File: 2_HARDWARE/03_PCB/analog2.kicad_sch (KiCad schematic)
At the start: 21 parts, among them U22 TPL0401B-10, U23 THS3491, U24 ADG1219BRJZ

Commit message: MINOR: Changed Boot Select Switches to Pull-Downs / Pull Up DNI and continued layout.
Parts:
- renumbered R75 to R76, R76 to R77, R6 to R78, R98 to R79, R77 to R80, R78 to R81, R79 to R82, R80 to R83, R81 to R84
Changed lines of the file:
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@@
 		(dnp no)
 		(fields_autoplaced yes)
-		(property "Reference" "#PWR0274"
+		(property "Reference" "#PWR0270"
 			(at 152.4 104.14 0)
 			(effects
@@
 			(project "arb"
 				(path "/866ef9be-3b01-4288-a6e0-a2357aa17e50/e46c6640-71a3-4b78-b602-0f6be9676e36"
-					(reference "#PWR0274")
+					(reference "#PWR0270")
 					(unit 1)
 				)
@@
 		(dnp yes)
 		(fields_autoplaced yes)
-		(property "Reference" "R77"
+		(property "Reference" "R80"
 			(at 154.94 144.7799 0)
 			(effects
@@
 			(project "arb"
 				(path "/866ef9be-3b01-4288-a6e0-a2357aa17e50/e46c6640-71a3-4b78-b602-0f6be9676e36"
-					(reference "R77")
+					(reference "R80")
 					(unit 1)
 				)
@@
 		(dnp no)
 		(fields_autoplaced yes)
-		(property "Reference" "#PWR0275"
+		(property "Reference" "#PWR0271"
 			(at 152.4 154.94 0)
 			(effects
@@
 			(project "arb"
 				(path "/866ef9be-3b01-4288-a6e0-a2357aa17e50/e46c6640-71a3-4b78-b602-0f6be9676e36"
-					(reference "#PWR0275")
+					(reference "#PWR0271")
 					(unit 1)
 				)
@@
 		(dnp no)
 		(fields_autoplaced yes)
-		(property "Reference" "#PWR0271"
+		(property "Reference" "#PWR0267"
 			(at 110.49 97.79 0)
 			(effects
@@
 			(project "arb"
 				(path "/866ef9be-3b01-4288-a6e0-a2357aa17e50/e46c6640-71a3-4b78-b602-0f6be9676e36"
-					(reference "#PWR0271")
+					(reference "#PWR0267")
 					(unit 1)
 				)
@@
 		(dnp no)
 		(fields_autoplaced yes)
-		(property "Reference" "R79"
+		(property "Reference" "R82"
 			(at 184.15 87.6299 0)
 			(effects
@@
 			(project "arb"
 				(path "/866ef9be-3b01-4288-a6e0-a2357aa17e50/e46c6640-71a3-4b78-b602-0f6be9676e36"
-					(reference "R79")
+					(reference "R82")
 					(unit 1)
 				)
@@
 		(dnp no)
 		(fields_autoplaced yes)
-		(property "Reference" "#PWR0273"
+		(property "Reference" "#PWR0269"
 			(at 144.78 154.94 0)
 			(effects
@@
 			(project "arb"
 				(path "/866ef9be-3b01-4288-a6e0-a2357aa17e50/e46c6640-71a3-4b78-b602-0f6be9676e36"
-					(reference "#PWR0273")
+					(reference "#PWR0269")
 					(unit 1)
 				)
@@
 		(on_board yes)
 		(dnp no)
-		(property "Reference" "#PWR0276"
+		(property "Reference" "#PWR0272"
 			(at 153.67 72.39 0)
 			(effects
@@
 			(project "arb"
 				(path "/866ef9be-3b01-4288-a6e0-a2357aa17e50/e46c6640-71a3-4b78-b602-0f6be9676e36"
-					(reference "#PWR0276")
+					(reference "#PWR0272")
 					(unit 1)
 				)
@@
 		(dnp no)
 		(fields_autoplaced yes)
-		(property "Reference" "R6"
+		(property "Reference" "R78"
 			(at 71.12 80.01 90)
 			(effects
@@
 			(project "arb"
 				(path "/866ef9be-3b01-4288-a6e0-a2357aa17e50/e46c6640-71a3-4b78-b602-0f6be9676e36"
-					(reference "R6")
+					(reference "R78")
 					(unit 1)
 				)
@@
 		(dnp no)
 		(fields_autoplaced yes)
-		(property "Reference" "#PWR0272"
+		(property "Reference" "#PWR0268"
 			(at 115.57 104.14 0)
 			(effects
@@
 			(project "arb"
 				(path "/866ef9be-3b01-4288-a6e0-a2357aa17e50/e46c6640-71a3-4b78-b602-0f6be9676e36"
-					(reference "#PWR0272")
+					(reference "#PWR0268")
 					(unit 1)
 				)
@@
 		(dnp no)
 		(fields_autoplaced yes)
-		(property "Reference" "R78"
+		(property "Reference" "R81"
 			(at 163.83 133.35 90)
 			(effects
@@
 			(project "arb"
 				(path "/866ef9be-3b01-4288-a6e0-a2357aa17e50/e46c6640-71a3-4b78-b602-0f6be9676e36"
-					(reference "R78")
+					(reference "R81")
 					(unit 1)
 				)
@@
 		(on_board yes)
 		(dnp no)
-		(property "Reference" "#PWR0269"
+		(property "Reference" "#PWR0265"
 			(at 106.68 78.74 0)
 			(effects
@@
 			(project "arb"
 				(path "/866ef9be-3b01-4288-a6e0-a2357aa17e50/e46c6640-71a3-4b78-b602-0f6be9676e36"
-					(reference "#PWR0269")
+					(reference "#PWR0265")
 					(unit 1)
 				)
@@
 		(dnp no)
 		(fields_autoplaced yes)
-		(property "Reference" "#PWR0264"
+		(property "Reference" "#PWR0260"
 			(at 81.28 101.6 0)
 			(effects
@@
 			(project "arb"
 				(path "/866ef9be-3b01-4288-a6e0-a2357aa17e50/e46c6640-71a3-4b78-b602-0f6be9676e36"
-					(reference "#PWR0264")
+					(reference "#PWR0260")
 					(unit 1)
 				)
@@
 		(dnp no)
 		(fields_autoplaced yes)
-		(property "Reference" "R80"
+		(property "Reference" "R83"
 			(at 187.96 133.35 90)
 			(effects
@@
 			(project "arb"
 				(path "/866ef9be-3b01-4288-a6e0-a2357aa17e50/e46c6640-71a3-4b78-b602-0f6be9676e36"
-					(reference "R80")
+					(reference "R83")
 					(unit 1)
 				)
@@
 		(dnp no)
 		(fields_autoplaced yes)
-		(property "Reference" "#PWR0280"
+		(property "Reference" "#PWR0276"
 			(at 181.61 97.79 0)
 			(effects
@@
 			(project "arb"
 				(path "/866ef9be-3b01-4288-a6e0-a2357aa17e50/e46c6640-71a3-4b78-b602-0f6be9676e36"
-					(reference "#PWR0280")
+					(reference "#PWR0276")
 					(unit 1)
 				)
@@
 		(dnp no)
 		(fields_autoplaced yes)
-		(property "Reference" "#PWR0278"
+		(property "Reference" "#PWR0274"
 			(at 157.48 97.79 0)
 			(effects
@@
 			(project "arb"
 				(path "/866ef9be-3b01-4288-a6e0-a2357aa17e50/e46c6640-71a3-4b78-b602-0f6be9676e36"
-					(reference "#PWR0278")
+					(reference "#PWR0274")
 					(unit 1)
 				)
@@
 		(dnp no)
 		(fields_autoplaced yes)
-		(property "Reference" "R76"
+		(property "Reference" "R77"
 			(at 64.77 114.2999 0)
 			(effects
@@
 			(project "arb"
 				(path "/866ef9be-3b01-4288-a6e0-a2357aa17e50/e46c6640-71a3-4b78-b602-0f6be9676e36"
-					(reference "R76")
+					(reference "R77")
 					(unit 1)
 				)
@@
 		(dnp no)
 		(fields_autoplaced yes)
-		(property "Reference" "#PWR0262"
+		(property "Reference" "#PWR0258"
 			(at 53.34 116.84 0)
 			(effects
@@
 			(project "arb"
 				(path "/866ef9be-3b01-4288-a6e0-a2357aa17e50/e46c6640-71a3-4b78-b602-0f6be9676e36"
-					(reference "#PWR0262")
+					(reference "#PWR0258")
 					(unit 1)
 				)
@@
 		(dnp no)
 		(fields_autoplaced yes)
-		(property "Reference" "R81"
+		(property "Reference" "R84"
 			(at 217.17 74.93 90)
 			(effects
@@
 			(project "arb"
 				(path "/866ef9be-3b01-4288-a6e0-a2357aa17e50/e46c6640-71a3-4b78-b602-0f6be9676e36"
-					(reference "R81")
+					(reference "R84")
 					(unit 1)
 				)
@@
 		(dnp no)
 		(fields_autoplaced yes)
-		(property "Reference" "R98"
+		(property "Reference" "R79"
 			(at 81.6066 80.01 90)
 			(effects
@@
 			(project "arb"
 				(path "/866ef9be-3b01-4288-a6e0-a2357aa17e50/e46c6640-71a3-4b78-b602-0f6be9676e36"
-					(reference "R98")
+					(reference "R79")
 					(unit 1)
 				)
@@
 		(on_board yes)
 		(dnp no)
-		(property "Reference" "#PWR0279"
+		(property "Reference" "#PWR0275"
 			(at 160.02 97.79 0)
 			(effects
@@
 			(project "arb"
 				(path "/866ef9be-3b01-4288-a6e0-a2357aa17e50/e46c6640-71a3-4b78-b602-0f6be9676e36"
-					(reference "#PWR0279")
+					(reference "#PWR0275")
 					(unit 1)
 				)
@@
 		(dnp no)
 		(fields_autoplaced yes)
-		(property "Reference" "#PWR0268"
+		(property "Reference" "#PWR0264"
 			(at 105.41 104.14 0)
 			(effects
@@
 			(project "arb"
 				(path "/866ef9be-3b01-4288-a6e0-a2357aa17e50/e46c6640-71a3-4b78-b602-0f6be9676e36"
-					(reference "#PWR0268")
+					(reference "#PWR0264")
 					(unit 1)
 				)
@@
 		(dnp no)
 		(fields_autoplaced yes)
-		(property "Reference" "#PWR0263"
+		(property "Reference" "#PWR0259"
 			(at 62.23 116.84 0)
 			(effects
@@
 			(project "arb"
 				(path "/866ef9be-3b01-4288-a6e0-a2357aa17e50/e46c6640-71a3-4b78-b602-0f6be9676e36"
-					(reference "#PWR0263")
+					(reference "#PWR0259")
 					(unit 1)
 				)
@@
 		(dnp no)
 		(fields_autoplaced yes)
-		(property "Reference" "#PWR0265"
+		(property "Reference" "#PWR0261"
 			(at 81.28 146.05 0)
 			(effects
@@
 			(project "arb"
 				(path "/866ef9be-3b01-4288-a6e0-a2357aa17e50/e46c6640-71a3-4b78-b602-0f6be9676e36"
-					(reference "#PWR0265")
+					(reference "#PWR0261")
 					(unit 1)
 				)
@@
 		(dnp no)
 		(fields_autoplaced yes)
-		(property "Reference" "R75"
+		(property "Reference" "R76"
 			(at 55.88 114.2999 0)
 			(effects
@@
 			(project "arb"
 				(path "/866ef9be-3b01-4288-a6e0-a2357aa17e50/e46c6640-71a3-4b78-b602-0f6be9676e36"
-					(reference "R75")
+					(reference "R76")
 					(unit 1)
 				)
@@
 		(on_board yes)
 		(dnp no)
-		(property "Reference" "#PWR0266"
+		(property "Reference" "#PWR0262"
 			(at 85.09 109.22 0)
 			(effects
@@
 			(project "arb"
 				(path "/866ef9be-3b01-4288-a6e0-a2357aa17e50/e46c6640-71a3-4b78-b602-0f6be9676e36"
-					(reference "#PWR0266")
+					(reference "#PWR0262")
 					(unit 1)
 				)
@@
 		(dnp no)
 		(fields_autoplaced yes)
-		(property "Reference" "#PWR0277"
+		(property "Reference" "#PWR0273"
 			(at 157.48 63.5 0)
 			(effects
@@
 			(project "arb"
 				(path "/866ef9be-3b01-4288-a6e0-a2357aa17e50/e46c6640-71a3-4b78-b602-0f6be9676e36"
-					(reference "#PWR0277")
+					(reference "#PWR0273")
 					(unit 1)
 				)
@@
 		(dnp no)
 		(fields_autoplaced yes)
-		(property "Reference" "#PWR0270"
+		(property "Reference" "#PWR0266"
 			(at 110.49 69.85 0)
 			(effects
@@
 			(project "arb"
 				(path "/866ef9be-3b01-4288-a6e0-a2357aa17e50/e46c6640-71a3-4b78-b602-0f6be9676e36"
-					(reference "#PWR0270")
+					(reference "#PWR0266")
 					(unit 1)
 				)
@@
 		(dnp no)
 		(fields_autoplaced yes)
-		(property "Reference" "#PWR0281"
+		(property "Reference" "#PWR0277"
 			(at 222.25 95.25 0)
 			(effects
@@
 			(project "arb"
 				(path "/866ef9be-3b01-4288-a6e0-a2357aa17e50/e46c6640-71a3-4b78-b602-0f6be9676e36"
-					(reference "#PWR0281")
+					(reference "#PWR0277")
 					(unit 1)
 				)
@@
 		(on_board yes)
 		(dnp no)
-		(property "Reference" "#PWR0267"
+		(property "Reference" "#PWR0263"
 			(at 99.06 87.63 0)
 			(effects
@@
 			(project "arb"
 				(path "/866ef9be-3b01-4288-a6e0-a2357aa17e50/e46c6640-71a3-4b78-b602-0f6be9676e36"
-					(reference "#PWR0267")
-					(unit 1)
-				)
+					(reference "#PWR0263")
+					(unit 1)
+				)

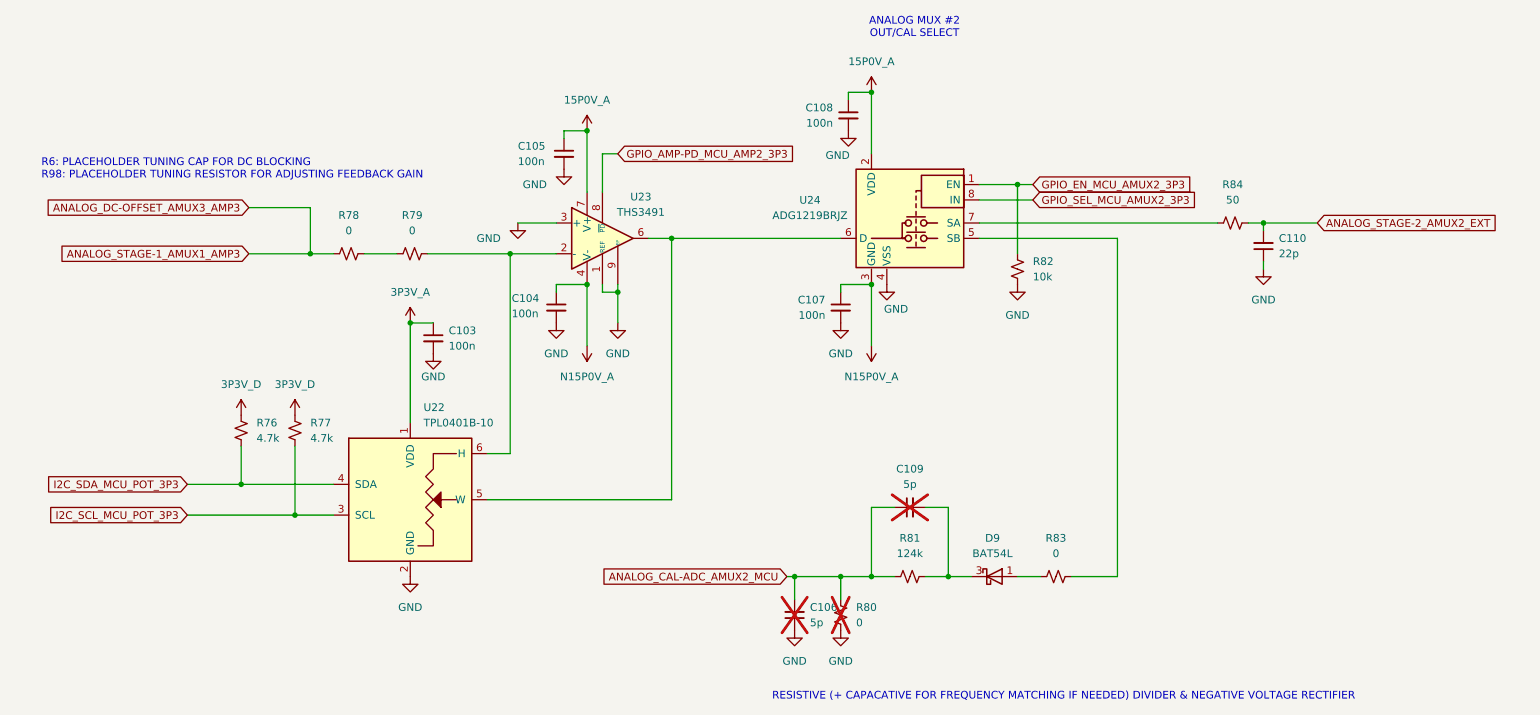
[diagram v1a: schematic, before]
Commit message: FEAT: Routed Analog and all Misc Signals. Routing is complete.
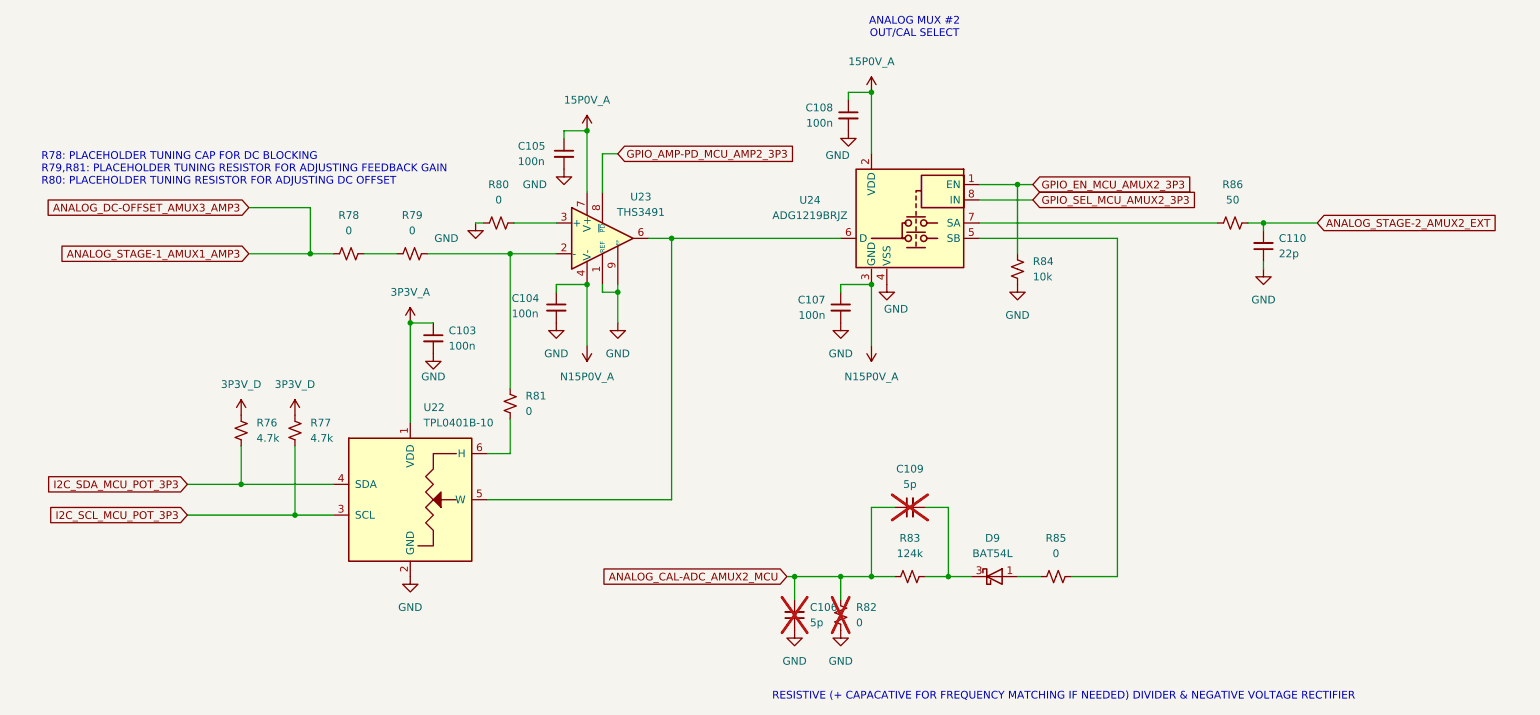
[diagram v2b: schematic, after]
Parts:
- added R80, R81: 0, Resistor_SMD:R_0603_1608Metric, symbol Device:R_Small_US
- renumbered R80 to R82, R81 to R83, R82 to R84, R83 to R85, R84 to R86
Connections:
- net GND: now also R80.1; no longer U23.3 (+)
- net at R79.2, U23.2 (-): now also R81.2; no longer U22.6 (H)
- new net: R81.1, U22.6 (H)
- new net: R80.2, U23.3 (+)
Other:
- note added: "R78: PLACEHOLDER TUNING CAP FOR DC BLOCKING R79,R81: PLACEHOLDER TUNING RESISTOR FOR ADJUSTING FEEDBACK GAIN R80: PLACEHOLDER TUNING RESISTOR FOR ADJUSTING DC OFFSET"
- note removed: "R6: PLACEHOLDER TUNING CAP FOR DC BLOCKING R98: PLACEHOLDER TUNING RESISTOR FOR ADJUSTING FEEDBACK GAIN"
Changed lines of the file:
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@@
 		)
 	)
-	(text "R6: PLACEHOLDER TUNING CAP FOR DC BLOCKING\nR98: PLACEHOLDER TUNING RESISTOR FOR ADJUSTING FEEDBACK GAIN"
+	(text "R78: PLACEHOLDER TUNING CAP FOR DC BLOCKING\nR79,R81: PLACEHOLDER TUNING RESISTOR FOR ADJUSTING FEEDBACK GAIN\nR80: PLACEHOLDER TUNING RESISTOR FOR ADJUSTING DC OFFSET"
 		(exclude_from_sim no)
 		(at 20.32 72.39 0)
@@
 	(wire
 		(pts
+			(xy 93.345 81.28) (xy 92.075 81.28)
+		)
+		(stroke
+			(width 0)
+			(type default)
+		)
+	)
+	(wire
+		(pts
 			(xy 181.61 74.93) (xy 181.61 86.36)
 		)
@@
 	(wire
 		(pts
+			(xy 97.79 108.585) (xy 97.79 86.36)
+		)
+		(stroke
+			(width 0)
+			(type default)
+		)
+	)
+	(wire
+		(pts
 			(xy 153.67 60.96) (xy 153.67 59.69)
 		)
@@
 	(wire
 		(pts
-			(xy 99.06 81.28) (xy 105.41 81.28)
-		)
-		(stroke
-			(width 0)
-			(type default)
-		)
-	)
-	(wire
-		(pts
 			(xy 157.48 91.44) (xy 152.4 91.44)
 		)
@@
 	(wire
 		(pts
-			(xy 97.79 119.38) (xy 97.79 86.36)
+			(xy 97.79 119.38) (xy 97.79 113.665)
 		)
 		(stroke
@@
 	(wire
 		(pts
+			(xy 98.425 81.28) (xy 105.41 81.28)
+		)
+		(stroke
+			(width 0)
+			(type default)
+		)
+	)
+	(wire
+		(pts
 			(xy 64.77 78.74) (xy 64.77 86.36)
 		)
@@
 		(dnp yes)
 		(fields_autoplaced yes)
-		(property "Reference" "R80"
+		(property "Reference" "R82"
 			(at 154.94 144.7799 0)
 			(effects
@@
 			(project "arb"
 				(path "/866ef9be-3b01-4288-a6e0-a2357aa17e50/e46c6640-71a3-4b78-b602-0f6be9676e36"
-					(reference "R80")
+					(reference "R82")
 					(unit 1)
 				)
@@
 		(dnp no)
 		(fields_autoplaced yes)
-		(property "Reference" "R82"
+		(property "Reference" "R84"
 			(at 184.15 87.6299 0)
 			(effects
@@
 			(project "arb"
 				(path "/866ef9be-3b01-4288-a6e0-a2357aa17e50/e46c6640-71a3-4b78-b602-0f6be9676e36"
-					(reference "R82")
+					(reference "R84")
+					(unit 1)
+				)
+			)
+		)
+	)
+	(symbol
+		(lib_id "Device:R_Small_US")
+		(at 97.79 111.125 180)
+		(unit 1)
+		(exclude_from_sim no)
+		(in_bom yes)
+		(on_board yes)
+		(dnp no)
+		(fields_autoplaced yes)
+		(property "Reference" "R81"
+			(at 100.33 109.8549 0)
+			(effects
+				(font
+					(size 1.27 1.27)
+				)
+				(justify right)
+			)
+		)
+		(property "Value" "0"
+			(at 100.33 112.3949 0)
+			(effects
+				(font
+					(size 1.27 1.27)
+				)
+				(justify right)
+			)
+		)
+		(property "Footprint" "Resistor_SMD:R_0603_1608Metric"
+			(at 97.79 111.125 0)
+			(effects
+				(font
+					(size 1.27 1.27)
+				)
+				(hide yes)
+			)
+		)
+		(property "Datasheet" "~"
+			(at 97.79 111.125 0)
+			(effects
+				(font
+					(size 1.27 1.27)
+				)
+				(hide yes)
+			)
+		)
+		(property "Description" "Resistor, small US symbol"
+			(at 97.79 111.125 0)
+			(effects
+				(font
+					(size 1.27 1.27)
+				)
+				(hide yes)
+			)
+		)
+		(property "Part Number" "0603WAJ0000T5E"
+			(at 97.79 111.125 0)
+			(effects
+				(font
+					(size 1.27 1.27)
+				)
+				(hide yes)
+			)
+		)
+		(property "LCSC" "C15402"
+			(at 97.79 111.125 0)
+			(effects
+				(font
+					(size 1.27 1.27)
+				)
+				(hide yes)
+			)
+		)
+		(pin "2"
+		)
+		(pin "1"
+		)
+		(instances
+			(project "arb"
+				(path "/866ef9be-3b01-4288-a6e0-a2357aa17e50/e46c6640-71a3-4b78-b602-0f6be9676e36"
+					(reference "R81")
 					(unit 1)
 				)
@@
 	(symbol
 		(lib_id "Device:R_Small_US")
+		(at 95.885 81.28 90)
+		(unit 1)
+		(exclude_from_sim no)
+		(in_bom yes)
+		(on_board yes)
+		(dnp no)
+		(fields_autoplaced yes)
+		(property "Reference" "R80"
+			(at 95.885 74.93 90)
+			(effects
+				(font
+					(size 1.27 1.27)
+				)
+			)
+		)
+		(property "Value" "0"
+			(at 95.885 77.47 90)
+			(effects
+				(font
+					(size 1.27 1.27)
+				)
+			)
+		)
+		(property "Footprint" "Resistor_SMD:R_0603_1608Metric"
+			(at 95.885 81.28 0)
+			(effects
+				(font
+					(size 1.27 1.27)
+				)
+				(hide yes)
+			)
+		)
+		(property "Datasheet" "~"
+			(at 95.885 81.28 0)
+			(effects
+				(font
+					(size 1.27 1.27)
+				)
+				(hide yes)
+			)
+		)
+		(property "Description" "Resistor, small US symbol"
+			(at 95.885 81.28 0)
+			(effects
+				(font
+					(size 1.27 1.27)
+				)
+				(hide yes)
+			)
+		)
+		(property "Part Number" "0603WAJ0000T5E"
+			(at 95.885 81.28 0)
+			(effects
+				(font
+					(size 1.27 1.27)
+				)
+				(hide yes)
+			)
+		)
+		(property "LCSC" "C15402"
+			(at 95.885 81.28 0)
+			(effects
+				(font
+					(size 1.27 1.27)
+				)
+				(hide yes)
+			)
+		)
+		(pin "2"
+		)
+		(pin "1"
+		)
+		(instances
+			(project "arb"
+				(path "/866ef9be-3b01-4288-a6e0-a2357aa17e50/e46c6640-71a3-4b78-b602-0f6be9676e36"
+					(reference "R80")
+					(unit 1)
+				)
+			)
+		)
+	)
+	(symbol
+		(lib_id "Device:R_Small_US")
 		(at 163.83 139.7 270)
 		(unit 1)
@@
 		(dnp no)
 		(fields_autoplaced yes)
-		(property "Reference" "R81"
+		(property "Reference" "R83"
 			(at 163.83 133.35 90)
 			(effects
@@
 			(project "arb"
 				(path "/866ef9be-3b01-4288-a6e0-a2357aa17e50/e46c6640-71a3-4b78-b602-0f6be9676e36"
-					(reference "R81")
+					(reference "R83")
 					(unit 1)
 				)
@@
 		(dnp no)
 		(fields_autoplaced yes)
-		(property "Reference" "R83"
+		(property "Reference" "R85"
 			(at 187.96 133.35 90)
 			(effects
@@
 			(project "arb"
 				(path "/866ef9be-3b01-4288-a6e0-a2357aa17e50/e46c6640-71a3-4b78-b602-0f6be9676e36"
-					(reference "R83")
+					(reference "R85")
 					(unit 1)
 				)
@@
 		(dnp no)
 		(fields_autoplaced yes)
-		(property "Reference" "R84"
+		(property "Reference" "R86"
 			(at 217.17 74.93 90)
 			(effects
@@
 			(project "arb"
 				(path "/866ef9be-3b01-4288-a6e0-a2357aa17e50/e46c6640-71a3-4b78-b602-0f6be9676e36"
-					(reference "R84")
+					(reference "R86")
 					(unit 1)
 				)
@@
 	(symbol
 		(lib_id "power:GND")
-		(at 99.06 81.28 0)
+		(at 92.075 81.28 0)
 		(unit 1)
 		(exclude_from_sim no)
@@
 		(dnp no)
 		(property "Reference" "#PWR0263"
-			(at 99.06 87.63 0)
+			(at 92.075 87.63 0)
 			(effects
 				(font
@@
 		)
 		(property "Value" "GND"
-			(at 94.234 83.82 0)
+			(at 87.249 83.82 0)
 			(effects
 				(font
@@
 		)
 		(property "Footprint" ""
-			(at 99.06 81.28 0)
+			(at 92.075 81.28 0)
 			(effects
 				(font
@@
 		)
 		(property "Datasheet" ""
-			(at 99.06 81.28 0)
+			(at 92.075 81.28 0)
 			(effects
 				(font
@@
 		)
 		(property "Description" "Power symbol creates a global label with name \"GND\" , ground"
-			(at 99.06 81.28 0)
+			(at 92.075 81.28 0)
 			(effects
 				(font
